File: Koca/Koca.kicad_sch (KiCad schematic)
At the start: 166 parts, among them J1 USB_C_Receptacle, J10 Conn_01x02_Pin, J11 Conn_01x02_Pin, J2 AudioJack4, J3 Conn_01x04_Pin, J4 Conn_01x04_Pin, J5 USB_C_Receptacle, J6 AudioJack4, J7 Conn_01x04_Pin, J8 Conn_01x04_Pin, J9 Conn_01x02_Pin, SW1 SW_Push, SW10 SW_Push, SW11 SW_Push, SW12 SW_Push, SW13 SW_Push, SW14 SW_Push, SW15 SW_Push, SW16 SW_Push, SW17 SW_Push, SW18 SW_Push, SW19 SW_Push, SW2 SW_Push, SW20 SW_Push, SW21 SW_Push, SW22 SW_Push, SW23 SW_Push, SW24 SW_Push, SW25 SW_Push, SW26 SW_Push, SW27 SW_Push, SW28 SW_Push, SW29 SW_Push, SW3 SW_Push, SW30 SW_Push, SW31 SW_Push, SW32 SW_Push, SW33 SW_Push, SW34 SW_Push, SW35 SW_Push, SW36 SW_Push, SW37 SW_Push, SW38 SW_Push, SW39 SW_Push, SW4 SW_Push, SW40 SW_Push, SW41 SW_Push, SW42 SW_Push, SW43 SW_Push, SW44 SW_Push, SW45 SW_Push, SW46 SW_Push, SW47 SW_Push, SW48 SW_Push, SW49 SW_Push, SW5 SW_Push, SW50 SW_Push, SW51 SW_Push, SW52 SW_Push, SW53 SW_Push, SW54 SW_Push, SW55 SW_Push, SW56 SW_Push, SW57 SW_Push, SW58 SW_Push, SW59 SW_Push, SW6 SW_Push, SW60 SW_Push, SW7 SW_Push, SW8 SW_Push, SW9 SW_Push, U1 AMS1117-3.3, U2 USBLC6-2SC6, U3 USBLC6-2SC6, U4 STM32F103RCTx, U5 AMS1117-3.3, U6 USBLC6-2SC6, U7 USBLC6-2SC6, U8 STM32F103RCTx, Y1 12Mhz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

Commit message: switch to direct matrix
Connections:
- net GND: now also SW1.1, SW10.1, SW11.1, SW12.1, SW13.1, SW14.1, SW15.1, SW16.1, SW17.1, SW18.1, SW19.1, SW2.1, SW20.1, SW21.1, SW22.1, SW23.1, SW24.1, SW25.1, SW26.1, SW27.1, SW28.1, SW29.1, SW3.1, SW30.1, SW4.1, SW5.1, SW6.1, SW8.1, SW9.1
- net GNDA: now also SW31.1, SW32.1, SW33.1, SW34.1, SW35.1, SW36.1, SW38.1, SW39.1, SW40.1, SW41.1, SW42.1, SW43.1, SW44.1, SW45.1, SW46.1, SW47.1, SW48.1, SW49.1, SW50.1, SW51.1, SW52.1, SW53.1, SW54.1, SW55.1, SW56.1, SW57.1, SW58.1, SW59.1, SW60.1
- removed net COMMON_L: SW1.1, SW10.1, SW11.1, SW12.1, SW13.1, SW14.1, SW15.1, SW16.1, SW17.1, SW18.1, SW19.1, SW2.1, SW20.1, SW21.1, SW22.1, SW23.1, SW24.1, SW25.1, SW26.1, SW27.1, SW28.1, SW29.1, SW3.1, SW30.1, SW4.1, SW5.1, SW6.1, SW8.1, SW9.1, U4.53 (PC12)
- removed net COMMON_R: SW31.1, SW32.1, SW33.1, SW34.1, SW35.1, SW36.1, SW38.1, SW39.1, SW40.1, SW41.1, SW42.1, SW43.1, SW44.1, SW45.1, SW46.1, SW47.1, SW48.1, SW49.1, SW50.1, SW51.1, SW52.1, SW53.1, SW54.1, SW55.1, SW56.1, SW57.1, SW58.1, SW59.1, SW60.1, U8.53 (PC12)
- no-connect marks 60 -> 62
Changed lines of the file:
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@@
 	(title_block
 		(title "Lily58 Koca")
-		(date "2025-01-21")
-		(rev "2")
+		(date "2025-01-29")
+		(rev "3")
 	)
 	(junction
@@
 	)
 	(junction
+		(at 45.72 350.52)
+		(diameter 0)
+		(color 0 0 0 0)
+	)
+	(junction
 		(at 372.11 120.65)
 		(diameter 0)
@@
 		(color 0 0 0 0)
 	)
+	(junction
+		(at 45.72 151.13)
+		(diameter 0)
+		(color 0 0 0 0)
+	)
 	(no_connect
 		(at 193.04 106.68)
@@
 	)
 	(no_connect
+		(at 453.39 128.27)
+	)
+	(no_connect
 		(at 193.04 99.06)
 	)
@@
 	)
 	(no_connect
+		(at 463.55 314.96)
+	)
+	(no_connect
 		(at 488.95 130.81)
 	)
@@
 	(wire
 		(pts
-			(xy 435.61 128.27) (xy 453.39 128.27)
-		)
-		(stroke
-			(width 0)
-			(type default)
-		)
-	)
-	(wire
-		(pts
 			(xy 444.5 251.46) (xy 444.5 250.19)
 		)
@@
 	(wire
 		(pts
+			(xy 45.72 350.52) (xy 45.72 354.33)
+		)
+		(stroke
+			(width 0)
+			(type default)
+		)
+	)
+	(wire
+		(pts
 			(xy 506.73 138.43) (xy 488.95 138.43)
 		)
@@
 	(wire
 		(pts
-			(xy 444.5 314.96) (xy 463.55 314.96)
-		)
-		(stroke
-			(width 0)
-			(type default)
-		)
-	)
-	(wire
-		(pts
 			(xy 429.26 113.03) (xy 453.39 113.03)
 		)
@@
 	(wire
 		(pts
+			(xy 45.72 151.13) (xy 45.72 156.21)
+		)
+		(stroke
+			(width 0)
+			(type default)
+		)
+	)
+	(wire
+		(pts
 			(xy 290.83 104.14) (xy 308.61 104.14)
 		)
@@
 		)
 	)
-	(global_label "COMMON_R"
-		(shape input)
-		(at 45.72 350.52 180)
-		(fields_autoplaced yes)
-		(effects
-			(font
-				(size 1.27 1.27)
-			)
-			(justify right)
-		)
-		(property "Intersheetrefs" "${INTERSHEET_REFS}"
-			(at 32.3329 350.52 0)
-			(effects
-				(font
-					(size 1.27 1.27)
-				)
-				(justify right)
-				(hide yes)
-			)
-		)
-	)
 	(global_label "R6"
 		(shape input)
@@
 		)
 	)
-	(global_label "COMMON_R"
-		(shape input)
-		(at 444.5 314.96 180)
-		(fields_autoplaced yes)
-		(effects
-			(font
-				(size 1.27 1.27)
-			)
-			(justify right)
-		)
-		(property "Intersheetrefs" "${INTERSHEET_REFS}"
-			(at 431.1129 314.96 0)
-			(effects
-				(font
-					(size 1.27 1.27)
-				)
-				(justify right)
-				(hide yes)
-			)
-		)
-	)
 	(global_label "L27"
 		(shape input)
@@
 		)
 	)
-	(global_label "COMMON_L"
-		(shape input)
-		(at 45.72 151.13 180)
-		(fields_autoplaced yes)
-		(effects
-			(font
-				(size 1.27 1.27)
-			)
-			(justify right)
-		)
-		(property "Intersheetrefs" "${INTERSHEET_REFS}"
-			(at 32.5748 151.13 0)
-			(effects
-				(font
-					(size 1.27 1.27)
-				)
-				(justify right)
-				(hide yes)
-			)
-		)
-	)
 	(global_label "L8"
 		(shape input)
@@
 		)
 	)
-	(global_label "COMMON_L"
-		(shape input)
-		(at 435.61 128.27 180)
-		(fields_autoplaced yes)
-		(effects
-			(font
-				(size 1.27 1.27)
-			)
-			(justify right)
-		)
-		(property "Intersheetrefs" "${INTERSHEET_REFS}"
-			(at 422.4648 128.27 0)
-			(effects
-				(font
-					(size 1.27 1.27)
-				)
-				(justify right)
-				(hide yes)
-			)
-		)
-	)
 	(global_label "R19"
 		(shape input)
@@
 	(symbol
 		(lib_id "power:GNDA")
+		(at 45.72 354.33 0)
+		(unit 1)
+		(exclude_from_sim no)
+		(in_bom yes)
+		(on_board yes)
+		(dnp no)
+		(fields_autoplaced yes)
+		(property "Reference" "#PWR059"
+			(at 45.72 360.68 0)
+			(effects
+				(font
+					(size 1.27 1.27)
+				)
+				(hide yes)
+			)
+		)
+		(property "Value" "GNDA"
+			(at 45.72 359.41 0)
+			(effects
+				(font
+					(size 1.27 1.27)
+				)
+			)
+		)
+		(property "Footprint" ""
+			(at 45.72 354.33 0)
+			(effects
+				(font
+					(size 1.27 1.27)
+				)
+				(hide yes)
+			)
+		)
+		(property "Datasheet" ""
+			(at 45.72 354.33 0)
+			(effects
+				(font
+					(size 1.27 1.27)
+				)
+				(hide yes)
+			)
+		)
+		(property "Description" "Power symbol creates a global label with name \"GNDA\" , analog ground"
+			(at 45.72 354.33 0)
+			(effects
+				(font
+					(size 1.27 1.27)
+				)
+				(hide yes)
+			)
+		)
+		(pin "1"
+		)
+		(instances
+			(project "Koca"
+				(path "/e4c6fdbb-fdc7-4ad4-a516-240d84cdc120"
+					(reference "#PWR059")
+					(unit 1)
+				)
+			)
+		)
+	)
+	(symbol
+		(lib_id "power:GNDA")
 		(at 414.02 280.67 0)
 		(unit 1)
@@
 					(unit 1)
 				)
+			)
+		)
+	)
+	(symbol
+		(lib_id "power:GND")
+		(at 45.72 156.21 0)
+		(unit 1)
+		(exclude_from_sim no)
+		(in_bom yes)
+		(on_board yes)
+		(dnp no)
+		(fields_autoplaced yes)
+		(property "Reference" "#PWR060"
+			(at 45.72 162.56 0)
+			(effects
+				(font
+					(size 1.27 1.27)
+				)
+				(hide yes)
+			)
+		)
+		(property "Value" "GND"
+			(at 45.72 161.29 0)
+			(effects
+				(font
+					(size 1.27 1.27)
+				)
+			)
+		)
+		(property "Footprint" ""
+			(at 45.72 156.21 0)
+			(effects
+				(font
+					(size 1.27 1.27)
+				)
+				(hide yes)
+			)
+		)
+		(property "Datasheet" ""
+			(at 45.72 156.21 0)
+			(effects
+				(font
+					(size 1.27 1.27)
+				)
+				(hide yes)
+			)
+		)
+		(property "Description" ""
+			(at 45.72 156.21 0)
+			(effects
+				(font
+					(size 1.27 1.27)
+				)
+				(hide yes)
+			)
+		)
+		(pin "1"
+		)
+		(instances
+			(project "Koca"
+				(path "/e4c6fdbb-fdc7-4ad4-a516-240d84cdc120"
+					(reference "#PWR060")
+					(unit 1)
+				)

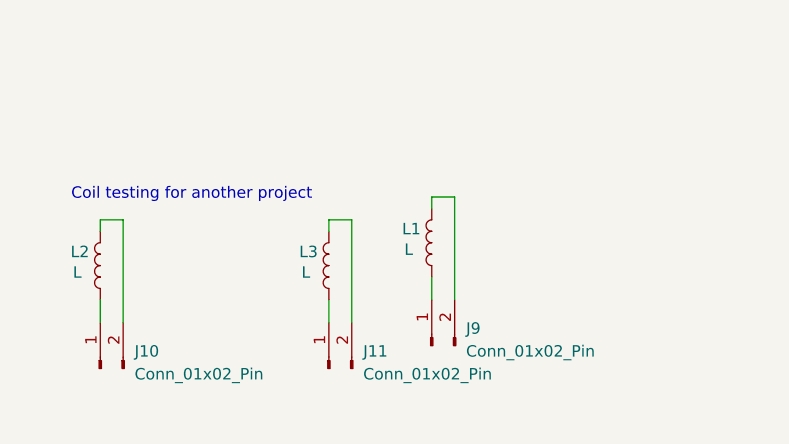
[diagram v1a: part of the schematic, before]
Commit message: Prepared files for double sided PCBA
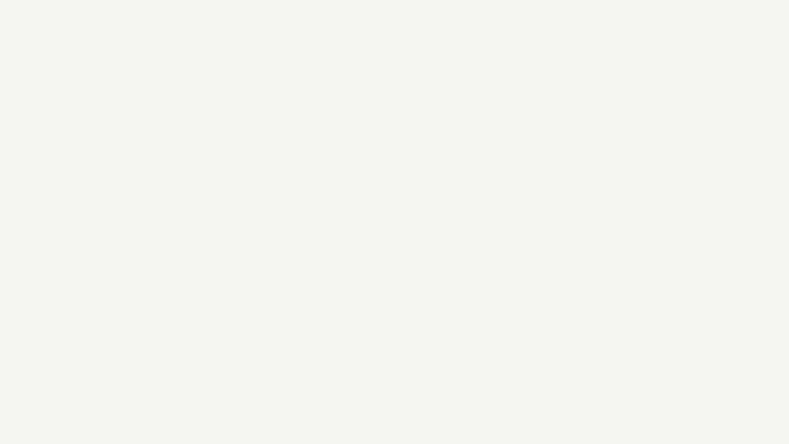
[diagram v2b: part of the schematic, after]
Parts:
- removed J10, J11, J9: Conn_01x02_Pin, Connector_PinSocket_2.54mm:PinSocket_1x02_P2.54mm_Vertical, symbol Connector:Conn_01x02_Pin
- removed L1: L, pcb_coils:COIL_GENERATOR5, symbol Device:L
- removed L2: L, pcb_coils:COIL_GENERATOR7, symbol Device:L
- removed L3: L, pcb_coils:COIL_GENERATOR10, symbol Device:L
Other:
- note removed: "Coil testing for another project"
